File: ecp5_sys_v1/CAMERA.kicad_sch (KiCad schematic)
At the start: 0 parts

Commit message: Worked on USB
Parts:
- added FPC1: 0.5-24P XGXJ-H2.0 119, EasyEDA:FPC-SMD_24P-P0.50_SHOU-HAN_XGXJ-H2.0, symbol EasyEDA:0.5-24PXGXJ-H2.0119
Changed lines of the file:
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@@
 	(generator_version "10.0")
 	(paper "A4")
+	(symbol
+		(lib_id "EasyEDA:0.5-24PXGXJ-H2.0119")
+		(at 132.08 86.36 0)
+		(unit 1)
+		(body_style 1)
+		(exclude_from_sim no)
+		(in_bom yes)
+		(on_board yes)
+		(in_pos_files yes)
+		(dnp no)
+		(fields_autoplaced yes)
+		(property "Reference" "FPC1"
+			(at 138.43 85.0899 0)
+			(show_name no)
+			(do_not_autoplace no)
+			(effects
+				(font
+					(size 1.27 1.27)
+				)
+				(justify left)
+			)
+		)
+		(property "Value" "0.5-24P XGXJ-H2.0 119"
+			(at 138.43 87.6299 0)
+			(show_name no)
+			(do_not_autoplace no)
+			(effects
+				(font
+					(size 1.27 1.27)
+				)
+				(justify left)
+			)
+		)
+		(property "Footprint" "EasyEDA:FPC-SMD_24P-P0.50_SHOU-HAN_XGXJ-H2.0"
+			(at 132.08 128.27 0)
+			(hide yes)
+			(show_name no)
+			(do_not_autoplace no)
+			(effects
+				(font
+					(size 1.27 1.27)
+				)
+			)
+		)
+		(property "Datasheet" "https://www.lcsc.com/datasheet/C2858298.pdf"
+			(at 132.08 130.81 0)
+			(hide yes)
+			(show_name no)
+			(do_not_autoplace no)
+			(effects
+				(font
+					(size 1.27 1.27)
+				)
+			)
+		)
+		(property "Description" ""
+			(at 132.08 86.36 0)
+			(hide yes)
+			(show_name no)
+			(do_not_autoplace no)
+			(effects
+				(font
+					(size 1.27 1.27)
+				)
+			)
+		)
+		(property "Manufacturer" "SHOU HAN(首韩)"
+			(at 132.08 133.35 0)
+			(hide yes)
+			(show_name no)
+			(do_not_autoplace no)
+			(effects
+				(font
+					(size 1.27 1.27)
+				)
+			)
+		)
+		(property "MPN" "0.5-24P XGXJ-H2.0 119"
+			(at 132.08 135.89 0)
+			(hide yes)
+			(show_name no)
+			(do_not_autoplace no)
+			(effects
+				(font
+					(size 1.27 1.27)
+				)
+			)
+		)
+		(property "LCSC Part" "C2858298"
+			(at 132.08 138.43 0)
+			(hide yes)
+			(show_name no)
+			(do_not_autoplace no)
+			(effects
+				(font
+					(size 1.27 1.27)
+				)
+			)
+		)
+		(pin "14"
+		)
+		(pin "1"
+		)
+		(pin "2"
+		)
+		(pin "4"
+		)
+		(pin "3"
+		)
+		(pin "5"
+		)
+		(pin "6"
+		)
+		(pin "7"
+		)
+		(pin "8"
+		)
+		(pin "9"
+		)
+		(pin "10"
+		)
+		(pin "11"
+		)
+		(pin "12"
+		)
+		(pin "13"
+		)
+		(pin "16"
+		)
+		(pin "25"
+		)
+		(pin "26"
+		)
+		(pin "17"
+		)
+		(pin "18"
+		)
+		(pin "21"
+		)
+		(pin "20"
+		)
+		(pin "15"
+		)
+		(pin "19"
+		)
+		(pin "22"
+		)
+		(pin "24"
+		)
+		(pin "23"
+		)
+		(instances
+			(project "ecp5_sys_v1"
+				(path "/08f8cf6b-931b-453e-b2e0-0373288a9134/9dcf90d5-2007-4f61-9b0b-281c7ff030ce"
+					(reference "FPC1")
+					(unit 1)
+				)
+			)
+		)
+	)
 )

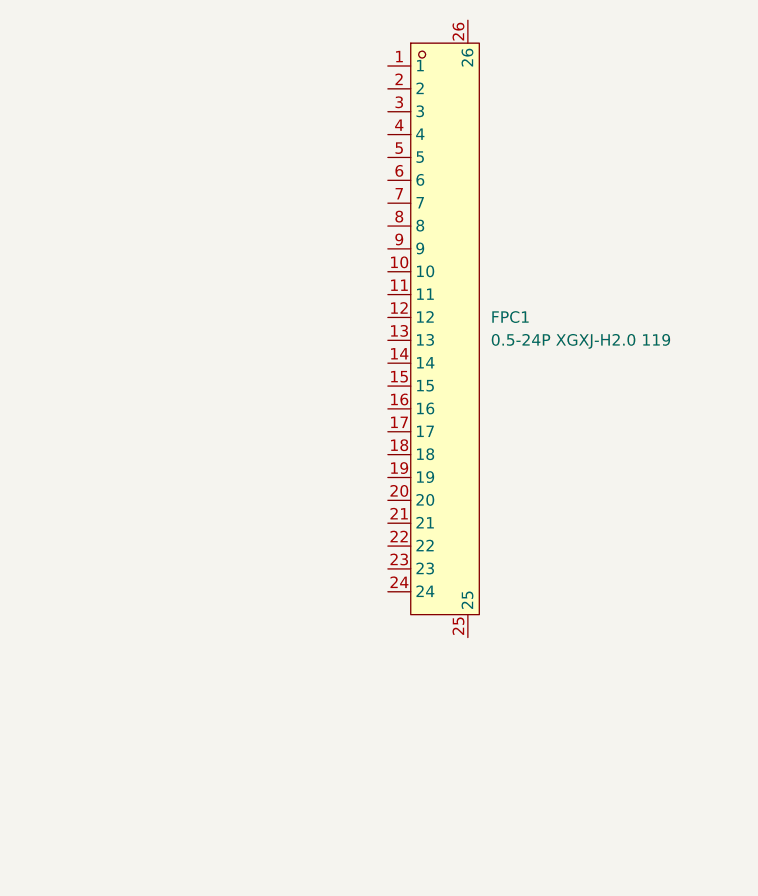
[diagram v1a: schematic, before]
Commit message: worked on power, should have external IC for sequencing and FPGA power is fine, started work in the CAMERA FPC, power 2V8 and 1V2 are there as LDOs, small package, should be fine.
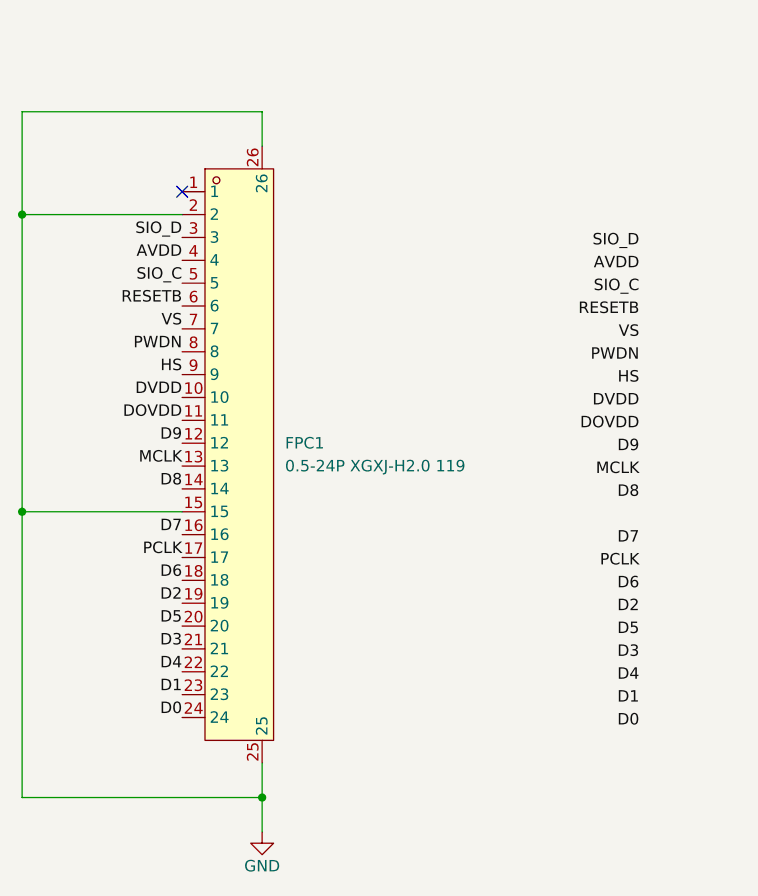
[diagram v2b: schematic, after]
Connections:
- net DVDD: now reaches FPC1.10
- net DOVDD: now reaches FPC1.11
- net D9: now reaches FPC1.12
- net MCLK: now reaches FPC1.13
- net D8: now reaches FPC1.14
- net GND: now reaches FPC1.15
- net GND: now also FPC1.2, FPC1.25, FPC1.26
- net D7: now reaches FPC1.16
- net PCLK: now reaches FPC1.17
- net D6: now reaches FPC1.18
- net D2: now reaches FPC1.19
- net D5: now reaches FPC1.20
- net D3: now reaches FPC1.21
- net D4: now reaches FPC1.22
- net D1: now reaches FPC1.23
- net D0: now reaches FPC1.24
- net SIO_D: now reaches FPC1.3
- net AVDD: now reaches FPC1.4
- net SIO_C: now reaches FPC1.5
- net RESETB: now reaches FPC1.6
- net VS: now reaches FPC1.7
- net PWDN: now reaches FPC1.8
- net HS: now reaches FPC1.9
- no-connect marks 0 -> 1
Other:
- moved on the sheet: FPC1
